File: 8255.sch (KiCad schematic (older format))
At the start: 14 parts, among them J1 Conn_01x08_Male, J2 Conn_01x08_Male, J3 Conn_01x08_Male, J4 Conn_01x08_Male, J5 Conn_01x08_Male, J6 Conn_01x08_Male, J7 Conn_01x08_Male, J8 Conn_01x08_Male, J9 Conn_01x08_Male, U10 8255, U11 8255, U12 8255, U8 PAL16L8, U9 4002

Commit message: made some modifications
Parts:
- removed U9: 4002, symbol 4xxx:4002
- added U? (x2): 74AHC1G08, symbol 74xGxx:74AHC1G08
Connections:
- wire segments 137 -> 141
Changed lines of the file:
@@
 Text GLabel 3500 6100 2    50   Input ~ 0
 A12
-$Comp
-L 4xxx:4002 U9
-U 1 1 608BEE6D
-P 2600 7350
-F 0 "U9" H 2600 7725 50  0000 C CNN
-F 1 "4002" H 2600 7634 50  0000 C CNN
-F 2 "" H 2600 7350 50  0001 C CNN
-F 3 "http://www.intersil.com/content/dam/Intersil/documents/cd40/cd4000bms-01bms-02bms-25bms.pdf" H 2600 7350 50  0001 C CNN
-	1    2600 7350
-	1    0    0    -1
-$EndComp
 Text GLabel 3500 5800 2    50   Input ~ 0
 A15
-Text GLabel 2300 7200 0    50   Input ~ 0
+Text GLabel 2250 7150 0    50   Input ~ 0
 A16
-Text GLabel 2300 7300 0    50   Input ~ 0
+Text GLabel 2250 7250 0    50   Input ~ 0
 A17
-Text GLabel 2300 7400 0    50   Input ~ 0
+Text GLabel 2250 7450 0    50   Input ~ 0
 A18
-Text GLabel 2300 7500 0    50   Input ~ 0
+Text GLabel 2250 7550 0    50   Input ~ 0
 A19
 Text Label 3350 6450 0    50   ~ 0
@@
 Wire Wire Line
 	3500 7350 2900 7350
-Wire Bus Line
-	2300 6850 2300 7500
 Text Label 2250 5150 0    50   ~ 0
 A[0:19]
@@
 	1    0    0    -1
 $EndComp
+$Comp
+L 74xGxx:74AHC1G08 U?
+U 1 1 60B21797
+P 2550 7200
+F 0 "U?" H 2525 7467 50  0000 C CNN
+F 1 "74AHC1G08" H 2525 7376 50  0000 C CNN
+F 2 "" H 2550 7200 50  0001 C CNN
+F 3 "http://www.ti.com/lit/sg/scyt129e/scyt129e.pdf" H 2550 7200 50  0001 C CNN
+	1    2550 7200
+	1    0    0    -1
+$EndComp
+$Comp
+L 74xGxx:74AHC1G08 U?
+U 1 1 60B2E03E
+P 2550 7500
+F 0 "U?" H 2525 7767 50  0000 C CNN
+F 1 "74AHC1G08" H 2525 7676 50  0000 C CNN
+F 2 "" H 2550 7500 50  0001 C CNN
+F 3 "http://www.ti.com/lit/sg/scyt129e/scyt129e.pdf" H 2550 7500 50  0001 C CNN
+	1    2550 7500
+	1    0    0    -1
+$EndComp
+Wire Wire Line
+	2800 7200 2900 7200
+Wire Wire Line
+	2800 7500 2900 7500
+Wire Wire Line
+	2900 7200 2900 7350
+Connection ~ 2900 7350
+Wire Wire Line
+	2900 7350 2900 7500
 Wire Wire Line
 	2200 6400 2350 6400

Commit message: made final adjustments to all the designes
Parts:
- removed U? (x2): 74AHC1G08, symbol 74xGxx:74AHC1G08
- added C201, C202, C203: 0.1uF, Capacitor_SMD:CP_Elec_3x5.3, symbol Device:C
- added U201: 74LS21, Package_DIP:DIP-14_W7.62mm_SMDSocket_SmallPads, symbol 74xx:74LS21
- J201: renamed from J1; footprint (none) -> Connector_JST:JST_GH_BM08B-GHS-TBT_1x08-1MP_P1.25mm_Vertical
- J202: renamed from J2; footprint (none) -> Connector_JST:JST_GH_BM08B-GHS-TBT_1x08-1MP_P1.25mm_Vertical
- J203: renamed from J3; footprint (none) -> Connector_JST:JST_GH_BM08B-GHS-TBT_1x08-1MP_P1.25mm_Vertical
- J204: renamed from J4; footprint (none) -> Connector_JST:JST_GH_BM08B-GHS-TBT_1x08-1MP_P1.25mm_Vertical
- J205: renamed from J5; footprint (none) -> Connector_JST:JST_GH_BM08B-GHS-TBT_1x08-1MP_P1.25mm_Vertical
- J206: renamed from J6; footprint (none) -> Connector_JST:JST_GH_BM08B-GHS-TBT_1x08-1MP_P1.25mm_Vertical
- J207: renamed from J7; footprint (none) -> Connector_JST:JST_GH_BM08B-GHS-TBT_1x08-1MP_P1.25mm_Vertical
- J208: renamed from J8; footprint (none) -> Connector_JST:JST_GH_BM08B-GHS-TBT_1x08-1MP_P1.25mm_Vertical
- J209: renamed from J9; footprint (none) -> Connector_JST:JST_GH_BM08B-GHS-TBT_1x08-1MP_P1.25mm_Vertical
- U202: renamed from U8; footprint (none) -> Package_DIP:DIP-20_W8.89mm_SMDSocket_LongPads
- renumbered U10 to U203, U11 to U204, U12 to U205
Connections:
- net A16: now also U201.1
- net A17: now also U201.2
- net A18: now also U201.4
- net A19: now also U201.5
- net GND: now also C201.1, C202.1, C203.1, U201.7 (GND)
- net VCC: now also C201.2, C202.2, C203.2, U201.14 (VCC)
- net at U202.13 (IO7): now also U201.6

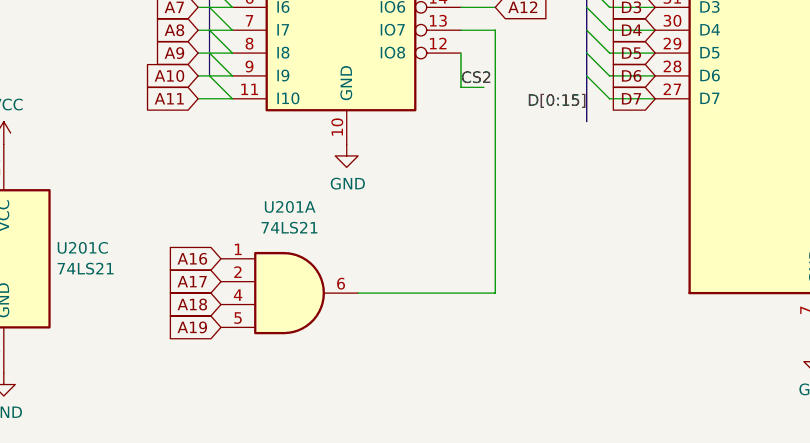
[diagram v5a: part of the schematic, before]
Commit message: adjusted and incorperated 8dipswitch to pcb
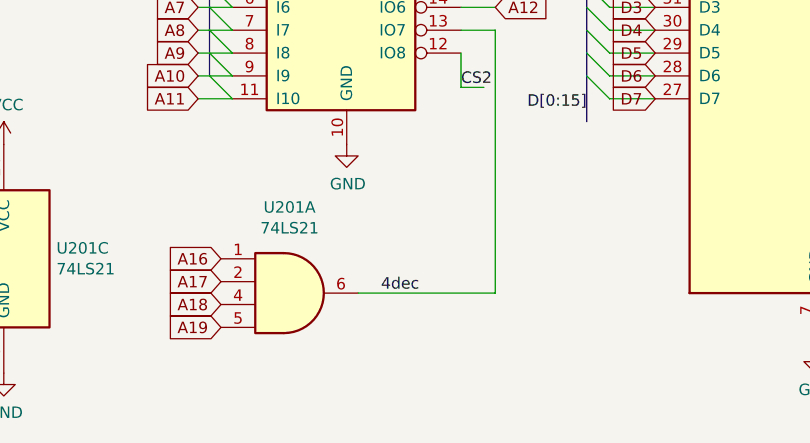
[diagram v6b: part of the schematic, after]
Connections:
- net 4dec: now reaches U201.6, U202.13 (IO7)
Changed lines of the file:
@@
 $Descr A4 11693 8268
 encoding utf-8
-Sheet 2 8
+Sheet 2 9
 Title ""
 Date ""
@@
 Wire Bus Line
 	2250 5050 2250 6400
+Text Label 3000 7350 0    50   ~ 0
+4dec
 $EndSCHEMATC
